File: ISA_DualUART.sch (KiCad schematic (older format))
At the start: 74 parts, among them J1 ISA BUS, J10 Parallel Port, J2 ADDR_IRQ, J3 UART1_SEL, J4 UART2_SEL, J6 Serial 2 IDC, J7 Serial 1 DB9, J9 Parport IRQ Select, U1 74LS138, U11 74LS30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

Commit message: Rerouted, now serial connector has shield to gnd
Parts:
- removed J7: Serial 1 DB9, Connector_Dsub:DSUB-9_Male_Horizontal_P2.77x2.84mm_EdgePinOffset7.70mm_Housed_MountingHolesOffset9.12mm, symbol Connector:DB9_Male
- added J7: Serial 1 DB9, Connector_Dsub:DSUB-9_Male_Horizontal_P2.77x2.84mm_EdgePinOffset7.70mm_Housed_MountingHolesOffset9.12mm, symbol Connector:DB9_Male_MountingHoles
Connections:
- wire segments 721 -> 722
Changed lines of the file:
@@
 	1500 9250 2300 9250
-$Comp
-L Connector:DB9_Male J7
-U 1 1 60F46B7A
-P 20700 3850
-F 0 "J7" H 20880 3896 50  0000 L CNN
-F 1 "Serial 1 DB9" H 20880 3805 50  0000 L CNN
-F 2 "Connector_Dsub:DSUB-9_Male_Horizontal_P2.77x2.84mm_EdgePinOffset7.70mm_Housed_MountingHolesOffset9.12mm" H 20700 3850 50  0001 C CNN
-F 3 " ~" H 20700 3850 50  0001 C CNN
-	1    20700 3850
-	1    0    0    -1
-$EndComp
 $Comp
 L power:GND #PWR0134
@@
 Wire Notes Line
 	22700 14700 22700 5350
+$Comp
+L Connector:DB9_Male_MountingHoles J7
+U 1 1 603C93D6
+P 20700 3850
+F 0 "J7" H 20880 3852 50  0000 L CNN
+F 1 "Serial 1 DB9" H 20880 3761 50  0000 L CNN
+F 2 "Connector_Dsub:DSUB-9_Male_Horizontal_P2.77x2.84mm_EdgePinOffset7.70mm_Housed_MountingHolesOffset9.12mm" H 20700 3850 50  0001 C CNN
+F 3 " ~" H 20700 3850 50  0001 C CNN
+	1    20700 3850
+	1    0    0    -1
+$EndComp
+$Comp
+L power:GND #PWR?
+U 1 1 60471E81
+P 20700 4600
+F 0 "#PWR?" H 20700 4350 50  0001 C CNN
+F 1 "GND" H 20705 4427 50  0000 C CNN
+F 2 "" H 20700 4600 50  0001 C CNN
+F 3 "" H 20700 4600 50  0001 C CNN
+	1    20700 4600
+	1    0    0    -1
+$EndComp
+Wire Wire Line
+	20700 4450 20700 4600
 Wire Bus Line
 	13800 7800 13800 13500

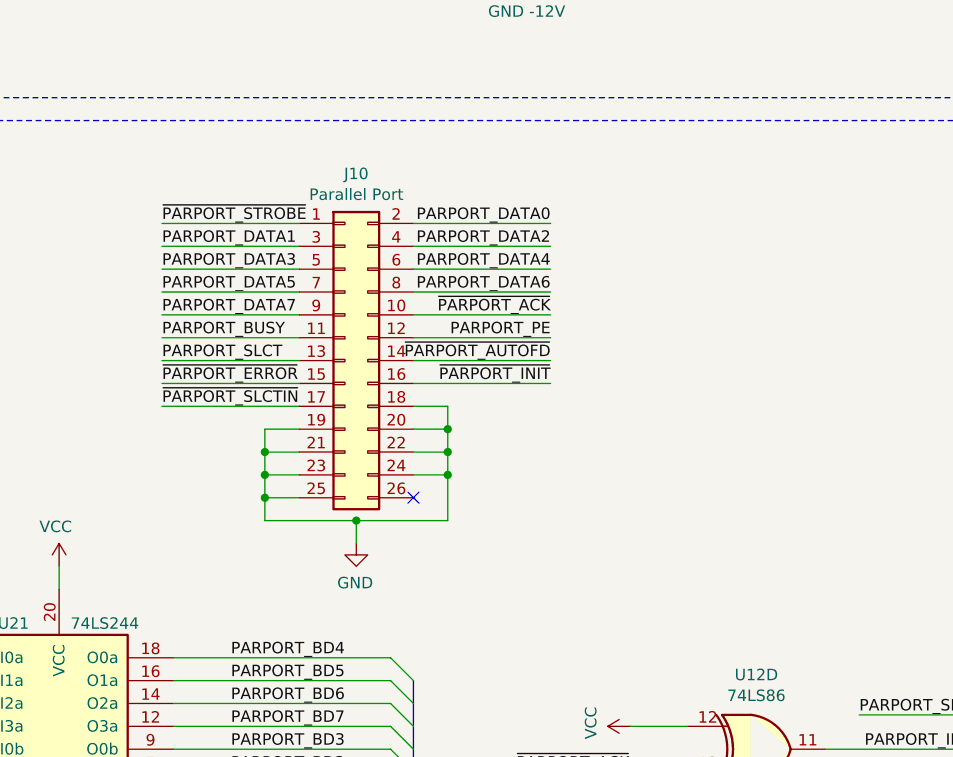
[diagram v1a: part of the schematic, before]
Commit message: Rewire parallel port connector
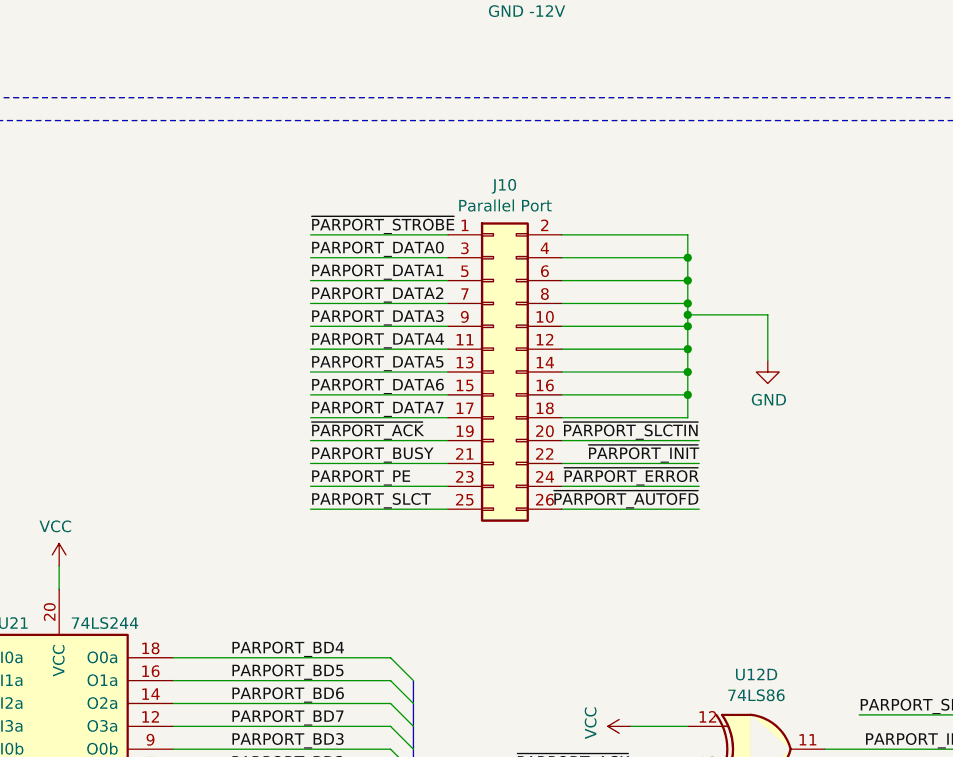
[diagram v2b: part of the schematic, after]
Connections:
- net GND: now also J10.10 (Pin_10), J10.12 (Pin_12), J10.14 (Pin_14), J10.16 (Pin_16), J10.2 (Pin_2), J10.4 (Pin_4), J10.6 (Pin_6), J10.8 (Pin_8); no longer J10.19 (Pin_19), J10.20 (Pin_20), J10.21 (Pin_21), J10.22 (Pin_22), J10.23 (Pin_23), J10.24 (Pin_24), J10.25 (Pin_25)
- net PARPORT_BUSY: now also J10.21 (Pin_21); no longer J10.11 (Pin_11)
- net PARPORT_DATA0: now also J10.3 (Pin_3); no longer J10.2 (Pin_2)
- net PARPORT_DATA1: now also J10.5 (Pin_5); no longer J10.3 (Pin_3)
- net PARPORT_DATA2: now also J10.7 (Pin_7); no longer J10.4 (Pin_4)
- net PARPORT_DATA3: now also J10.9 (Pin_9); no longer J10.5 (Pin_5)
- net PARPORT_DATA4: now also J10.11 (Pin_11); no longer J10.6 (Pin_6)
- net PARPORT_DATA5: now also J10.13 (Pin_13); no longer J10.7 (Pin_7)
- net PARPORT_DATA6: now also J10.15 (Pin_15); no longer J10.8 (Pin_8)
- net PARPORT_DATA7: now also J10.17 (Pin_17); no longer J10.9 (Pin_9)
- net PARPORT_PE: now also J10.23 (Pin_23); no longer J10.12 (Pin_12)
- net PARPORT_SLCT: now also J10.25 (Pin_25); no longer J10.13 (Pin_13)
- net ~PARPORT_ACK: now also J10.19 (Pin_19); no longer J10.10 (Pin_10)
- net ~PARPORT_AUTOFD: now also J10.26 (Pin_26); no longer J10.14 (Pin_14)
- net ~PARPORT_ERROR: now also J10.24 (Pin_24); no longer J10.15 (Pin_15)
- net ~PARPORT_INIT: now also J10.22 (Pin_22); no longer J10.16 (Pin_16)
- net ~PARPORT_SLCTIN: now also J10.20 (Pin_20); no longer J10.17 (Pin_17)
- no-connect marks 43 -> 42
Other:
- moved on the sheet: J10
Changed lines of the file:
@@
 Wire Bus Line
 	7650 13500 13800 13500
-$Comp
-L 74xx:74LS244 U21
-U 1 1 6EEE2F98
-P 12250 8200
-F 0 "U21" H 12050 8850 50  0000 C CNN
-F 1 "74LS244" H 12450 8850 50  0000 C CNN
-F 2 "Package_DIP:DIP-20_W7.62mm_LongPads" H 12250 8200 50  0001 C CNN
-F 3 "http://www.ti.com/lit/ds/symlink/sn74ls244.pdf" H 12250 8200 50  0001 C CNN
-	1    12250 8200
-	1    0    0    -1
-$EndComp
 Wire Wire Line
 	12250 7300 12250 7400
@@
 L Connector_Generic:Conn_02x13_Odd_Even J10
 U 1 1 7146EF36
-P 13500 6400
-F 0 "J10" H 13550 7217 50  0000 C CNN
-F 1 "Parallel Port" H 13550 7126 50  0000 C CNN
-F 2 "Connector_PinHeader_2.54mm:PinHeader_2x13_P2.54mm_Vertical" H 13500 6400 50  0001 C CNN
-F 3 "~" H 13500 6400 50  0001 C CNN
-	1    13500 6400
-	1    0    0    -1
-$EndComp
-NoConn ~ 13800 7000
-Wire Wire Line
-	13300 6700 13150 6700
-Wire Wire Line
-	13300 6800 13150 6800
-Wire Wire Line
-	13300 6900 13150 6900
-Wire Wire Line
-	13300 7000 13150 7000
-Wire Wire Line
-	13950 6600 13800 6600
-Wire Wire Line
-	13950 6700 13800 6700
-Wire Wire Line
-	13950 6800 13800 6800
-Wire Wire Line
-	13950 6900 13800 6900
-Wire Wire Line
-	13950 6600 13950 6700
-Wire Wire Line
-	13950 6700 13950 6800
-Connection ~ 13950 6700
-Wire Wire Line
-	13950 6800 13950 6900
-Connection ~ 13950 6800
-Wire Wire Line
-	13150 6700 13150 6800
-Wire Wire Line
-	13150 6800 13150 6900
-Connection ~ 13150 6800
-Wire Wire Line
-	13150 6900 13150 7000
-Connection ~ 13150 6900
-Wire Wire Line
-	13950 6900 13950 7100
-Wire Wire Line
-	13950 7100 13550 7100
-Wire Wire Line
-	13150 7100 13150 7000
-Connection ~ 13950 6900
-Connection ~ 13150 7000
-$Comp
-L power:GND #PWR0204
-U 1 1 72044B44
-P 13550 7200
-F 0 "#PWR0204" H 13550 6950 50  0001 C CNN
-F 1 "GND" H 13555 7027 50  0000 C CNN
-F 2 "" H 13550 7200 50  0001 C CNN
-F 3 "" H 13550 7200 50  0001 C CNN
-	1    13550 7200
-	-1   0    0    -1
-$EndComp
-Wire Wire Line
-	13550 7100 13550 7200
-Connection ~ 13550 7100
-Wire Wire Line
-	13550 7100 13150 7100
-Wire Wire Line
-	13300 5800 12700 5800
-Wire Wire Line
-	13300 5900 12700 5900
-Wire Wire Line
-	13300 6000 12700 6000
-Wire Wire Line
-	13300 6100 12700 6100
-Wire Wire Line
-	13300 6200 12700 6200
-Wire Wire Line
-	13300 6300 12700 6300
-Wire Wire Line
-	13300 6400 12700 6400
-Wire Wire Line
-	13300 6500 12700 6500
-Wire Wire Line
-	13300 6600 12700 6600
-Wire Wire Line
-	14400 5800 13800 5800
-Wire Wire Line
-	14400 5900 13800 5900
-Wire Wire Line
-	14400 6000 13800 6000
-Wire Wire Line
-	14400 6100 13800 6100
-Wire Wire Line
-	14400 6200 13800 6200
-Wire Wire Line
-	14400 6300 13800 6300
-Wire Wire Line
-	14400 6400 13800 6400
-Wire Wire Line
-	14400 6500 13800 6500
-Text Label 12700 5800 0    50   ~ 0
+P 14150 6450
+F 0 "J10" H 14200 7267 50  0000 C CNN
+F 1 "Parallel Port" H 14200 7176 50  0000 C CNN
+F 2 "Connector_PinHeader_2.54mm:PinHeader_2x13_P2.54mm_Vertical" H 14150 6450 50  0001 C CNN
+F 3 "~" H 14150 6450 50  0001 C CNN
+	1    14150 6450
+	1    0    0    -1
+$EndComp
+Wire Wire Line
+	13950 5850 13350 5850
+Wire Wire Line
+	13950 6050 13350 6050
+Wire Wire Line
+	13950 6250 13350 6250
+Wire Wire Line
+	13950 6450 13350 6450
+Wire Wire Line
+	13950 6650 13350 6650
+Wire Wire Line
+	13950 6850 13350 6850
+Wire Wire Line
+	13950 7050 13350 7050
+Wire Wire Line
+	14450 6950 15050 6950
+Wire Wire Line
+	14450 6750 15050 6750
+Wire Wire Line
+	13350 5950 13950 5950
+Wire Wire Line
+	13350 6150 13950 6150
+Wire Wire Line
+	13350 6350 13950 6350
+Wire Wire Line
+	13350 6550 13950 6550
+Wire Wire Line
+	13350 6750 13950 6750
+Wire Wire Line
+	13350 6950 13950 6950
+Wire Wire Line
+	15050 7050 14450 7050
+Wire Wire Line
+	15050 6850 14450 6850
+Text Label 13350 5850 0    50   ~ 0
 ~PARPORT_STROBE
-Text Label 12700 5900 0    50   ~ 0
+Text Label 13350 6050 0    50   ~ 0
 PARPORT_DATA1
-Text Label 12700 6000 0    50   ~ 0
+Text Label 13350 6250 0    50   ~ 0
 PARPORT_DATA3
-Text Label 12700 6100 0    50   ~ 0
+Text Label 13350 6450 0    50   ~ 0
 PARPORT_DATA5
-Text Label 12700 6200 0    50   ~ 0
+Text Label 13350 6650 0    50   ~ 0
 PARPORT_DATA7
-Text Label 14400 5800 2    50   ~ 0
+Text Label 13350 5950 0    50   ~ 0
 PARPORT_DATA0
-Text Label 14400 5900 2    50   ~ 0
+Text Label 13350 6150 0    50   ~ 0
 PARPORT_DATA2
-Text Label 14400 6000 2    50   ~ 0
+Text Label 13350 6350 0    50   ~ 0
 PARPORT_DATA4
-Text Label 14400 6100 2    50   ~ 0
+Text Label 13350 6550 0    50   ~ 0
 PARPORT_DATA6
-Text Label 12700 6300 0    50   ~ 0
+Text Label 13350 6850 0    50   ~ 0
 PARPORT_BUSY
-Text Label 12700 6400 0    50   ~ 0
+Text Label 13350 7050 0    50   ~ 0
 PARPORT_SLCT
-Text Label 12700 6500 0    50   ~ 0
+Text Label 15050 6950 2    50   ~ 0
 ~PARPORT_ERROR
-Text Label 12700 6600 0    50   ~ 0
+Text Label 15050 6750 2    50   ~ 0
 ~PARPORT_SLCTIN
-Text Label 14400 6200 2    50   ~ 0
+Text Label 13350 6750 0    50   ~ 0
 ~PARPORT_ACK
-Text Label 14400 6300 2    50   ~ 0
+Text Label 13350 6950 0    50   ~ 0
 PARPORT_PE
-Text Label 14400 6400 2    50   ~ 0
+Text Label 15050 7050 2    50   ~ 0
 ~PARPORT_AUTOFD
-Text Label 14400 6500 2    50   ~ 0
+Text Label 15050 6850 2    50   ~ 0
 ~PARPORT_INIT
 $Comp
@@
 Wire Wire Line
 	20700 4450 20700 4600
+Wire Wire Line
+	14450 5850 15000 5850
+Wire Wire Line
+	14450 5950 15000 5950
+Wire Wire Line
+	14450 6050 15000 6050
+Wire Wire Line
+	14450 6150 15000 6150
+Wire Wire Line
+	14450 6250 15000 6250
+Wire Wire Line
+	14450 6350 15000 6350
+Wire Wire Line
+	14450 6450 15000 6450
+Wire Wire Line
+	14450 6550 15000 6550
+Wire Wire Line
+	14450 6650 15000 6650
+Wire Wire Line
+	15000 5850 15000 5950
+Wire Wire Line
+	15000 6050 15000 5950
+Connection ~ 15000 5950
+Wire Wire Line
+	15000 6050 15000 6150
+Connection ~ 15000 6050
+Wire Wire Line
+	15000 6150 15000 6200
+Connection ~ 15000 6150
+Wire Wire Line
+	15000 6250 15000 6350
+Connection ~ 15000 6250
+Wire Wire Line
+	15000 6350 15000 6450
+Connection ~ 15000 6350
+Wire Wire Line
+	15000 6450 15000 6550
+Connection ~ 15000 6450
+Wire Wire Line
+	15000 6550 15000 6650
+Connection ~ 15000 6550
+Wire Wire Line
+	15000 6200 15350 6200
+Wire Wire Line
+	15350 6200 15350 6400
+Connection ~ 15000 6200
+Wire Wire Line
+	15000 6200 15000 6250
+$Comp
+L power:GND #PWR?
+U 1 1 635BB839
+P 15350 6400
+F 0 "#PWR?" H 15350 6150 50  0001 C CNN
+F 1 "GND" H 15355 6227 50  0000 C CNN
+F 2 "" H 15350 6400 50  0001 C CNN
+F 3 "" H 15350 6400 50  0001 C CNN
+	1    15350 6400
+	1    0    0    -1
+$EndComp
+$Comp
+L 74xx:74LS244 U21
+U 1 1 6EEE2F98
+P 12250 8200
+F 0 "U21" H 12050 8850 50  0000 C CNN
+F 1 "74LS244" H 12450 8850 50  0000 C CNN
+F 2 "Package_DIP:DIP-20_W7.62mm_LongPads" H 12250 8200 50  0001 C CNN
+F 3 "http://www.ti.com/lit/ds/symlink/sn74ls244.pdf" H 12250 8200 50  0001 C CNN
+	1    12250 8200
+	1    0    0    -1
+$EndComp
 Wire Bus Line
 	13800 7800 13800 13500

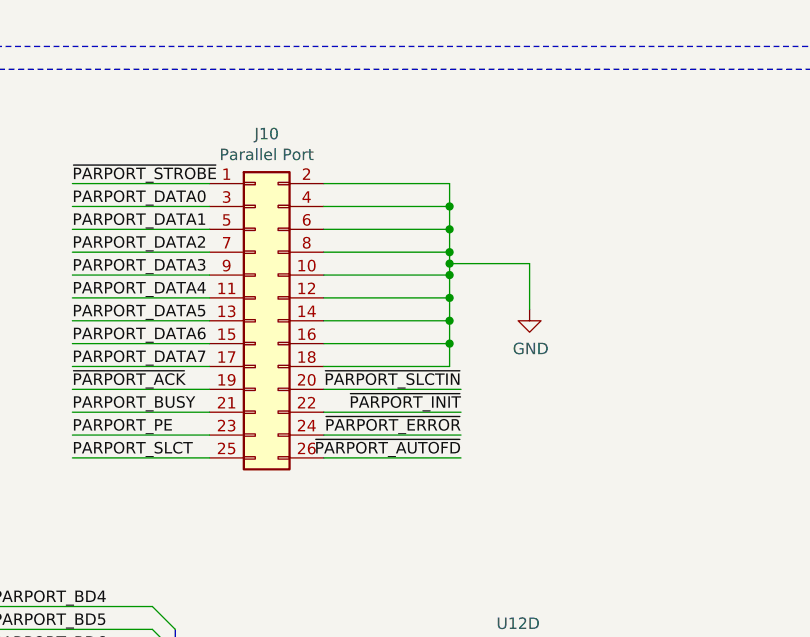
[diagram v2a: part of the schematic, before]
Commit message: Changed organization of parport connector
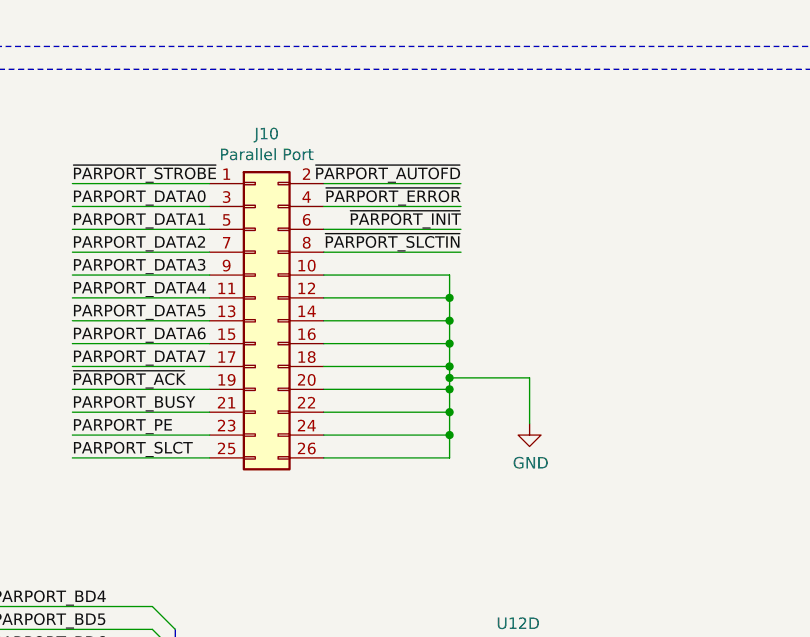
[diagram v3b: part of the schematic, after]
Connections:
- net GND: now also J10.20 (Pin_20), J10.22 (Pin_22), J10.24 (Pin_24), J10.26 (Pin_26); no longer J10.2 (Pin_2), J10.4 (Pin_4), J10.6 (Pin_6), J10.8 (Pin_8)
- net ~PARPORT_AUTOFD: now also J10.2 (Pin_2); no longer J10.26 (Pin_26)
- net ~PARPORT_ERROR: now also J10.4 (Pin_4); no longer J10.24 (Pin_24)
- net ~PARPORT_INIT: now also J10.6 (Pin_6); no longer J10.22 (Pin_22)
- net ~PARPORT_SLCTIN: now also J10.8 (Pin_8); no longer J10.20 (Pin_20)
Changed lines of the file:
@@
 	13950 7050 13350 7050
 Wire Wire Line
-	14450 6950 15050 6950
-Wire Wire Line
-	14450 6750 15050 6750
+	14450 5950 15050 5950
+Wire Wire Line
+	14450 6150 15050 6150
 Wire Wire Line
 	13350 5950 13950 5950
@@
 	13350 6950 13950 6950
 Wire Wire Line
-	15050 7050 14450 7050
-Wire Wire Line
-	15050 6850 14450 6850
+	15050 5850 14450 5850
+Wire Wire Line
+	15050 6050 14450 6050
 Text Label 13350 5850 0    50   ~ 0
 ~PARPORT_STROBE
@@
 Text Label 13350 7050 0    50   ~ 0
 PARPORT_SLCT
-Text Label 15050 6950 2    50   ~ 0
+Text Label 15050 5950 2    50   ~ 0
 ~PARPORT_ERROR
-Text Label 15050 6750 2    50   ~ 0
+Text Label 15050 6150 2    50   ~ 0
 ~PARPORT_SLCTIN
 Text Label 13350 6750 0    50   ~ 0
@@
 Text Label 13350 6950 0    50   ~ 0
 PARPORT_PE
-Text Label 15050 7050 2    50   ~ 0
+Text Label 15050 5850 2    50   ~ 0
 ~PARPORT_AUTOFD
-Text Label 15050 6850 2    50   ~ 0
+Text Label 15050 6050 2    50   ~ 0
 ~PARPORT_INIT
 $Comp
@@
 $EndComp
 $Comp
-L power:GND #PWR?
+L power:GND #PWR0146
 U 1 1 60471E81
 P 20700 4600
-F 0 "#PWR?" H 20700 4350 50  0001 C CNN
+F 0 "#PWR0146" H 20700 4350 50  0001 C CNN
 F 1 "GND" H 20705 4427 50  0000 C CNN
 F 2 "" H 20700 4600 50  0001 C CNN
@@
 	20700 4450 20700 4600
 Wire Wire Line
-	14450 5850 15000 5850
-Wire Wire Line
-	14450 5950 15000 5950
-Wire Wire Line
-	14450 6050 15000 6050
-Wire Wire Line
-	14450 6150 15000 6150
+	14450 7050 15000 7050
+Wire Wire Line
+	14450 6950 15000 6950
+Wire Wire Line
+	14450 6850 15000 6850
+Wire Wire Line
+	14450 6750 15000 6750
+Wire Wire Line
+	14450 6650 15000 6650
+Wire Wire Line
+	14450 6550 15000 6550
+Wire Wire Line
+	14450 6450 15000 6450
+Wire Wire Line
+	14450 6350 15000 6350
 Wire Wire Line
 	14450 6250 15000 6250
 Wire Wire Line
-	14450 6350 15000 6350
-Wire Wire Line
-	14450 6450 15000 6450
-Wire Wire Line
-	14450 6550 15000 6550
-Wire Wire Line
-	14450 6650 15000 6650
-Wire Wire Line
-	15000 5850 15000 5950
-Wire Wire Line
-	15000 6050 15000 5950
-Connection ~ 15000 5950
-Wire Wire Line
-	15000 6050 15000 6150
-Connection ~ 15000 6050
-Wire Wire Line
-	15000 6150 15000 6200
-Connection ~ 15000 6150
-Wire Wire Line
-	15000 6250 15000 6350
-Connection ~ 15000 6250
-Wire Wire Line
-	15000 6350 15000 6450
+	15000 7050 15000 6950
+Wire Wire Line
+	15000 6850 15000 6950
+Connection ~ 15000 6950
+Wire Wire Line
+	15000 6850 15000 6750
+Connection ~ 15000 6850
+Wire Wire Line
+	15000 6750 15000 6700
+Connection ~ 15000 6750
+Wire Wire Line
+	15000 6650 15000 6550
+Connection ~ 15000 6650
+Wire Wire Line
+	15000 6550 15000 6450
+Connection ~ 15000 6550
+Wire Wire Line
+	15000 6450 15000 6350
+Connection ~ 15000 6450
+Wire Wire Line
+	15000 6350 15000 6250
 Connection ~ 15000 6350
 Wire Wire Line
-	15000 6450 15000 6550
-Connection ~ 15000 6450
-Wire Wire Line
-	15000 6550 15000 6650
-Connection ~ 15000 6550
-Wire Wire Line
-	15000 6200 15350 6200
-Wire Wire Line
-	15350 6200 15350 6400
-Connection ~ 15000 6200
-Wire Wire Line
-	15000 6200 15000 6250
-$Comp
-L power:GND #PWR?
+	15000 6700 15350 6700
+Wire Wire Line
+	15350 6700 15350 6900
+Connection ~ 15000 6700
+Wire Wire Line
+	15000 6700 15000 6650
+$Comp
+L power:GND #PWR0147
 U 1 1 635BB839
-P 15350 6400
-F 0 "#PWR?" H 15350 6150 50  0001 C CNN
-F 1 "GND" H 15355 6227 50  0000 C CNN
-F 2 "" H 15350 6400 50  0001 C CNN
-F 3 "" H 15350 6400 50  0001 C CNN
-	1    15350 6400
-	1    0    0    -1
-$EndComp
+P 15350 6900
+F 0 "#PWR0147" H 15350 6650 50  0001 C CNN
+F 1 "GND" H 15355 6727 50  0000 C CNN
+F 2 "" H 15350 6900 50  0001 C CNN
+F 3 "" H 15350 6900 50  0001 C CNN
+	1    15350 6900
+	1    0    0    -1
+$EndComp

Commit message: Invert IRQ sensing to conform to AT specs
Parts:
- added R16: 4.7k, Resistor_THT:R_Axial_DIN0207_L6.3mm_D2.5mm_P10.16mm_Horizontal, symbol Device:R_Small
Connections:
- net PARPORT_IRQ: no longer U19.12
- net VCC: now also R16.1
- net ~PARPORT_ACK: now also U19.12, R16.2
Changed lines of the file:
@@
 	14750 8000 15000 8000
 Wire Wire Line
-	15000 8200 14250 8200
+	15000 8200 14750 8200
 Text Label 14250 8200 0    50   ~ 0
 ~PARPORT_ACK
@@
 Text Label 14550 9150 0    50   ~ 0
 ~PARPORT_IRQEN
-Wire Wire Line
-	16350 8100 16350 8350
-Wire Wire Line
-	16350 8350 14750 8350
-Wire Wire Line
-	14750 8350 14750 8750
 Wire Wire Line
 	14750 8750 15000 8750
@@
 Wire Wire Line
 	18800 8700 16350 8700
-Wire Wire Line
-	16350 8700 16350 8350
-Connection ~ 16350 8350
 Text Label 18050 9200 0    50   ~ 0
 ~PARPORT_STROBE
@@
 	1    0    0    -1
 $EndComp
+$Comp
+L Device:R_Small R16
+U 1 1 63A381BF
+P 14450 8750
+F 0 "R16" V 14550 8850 50  0000 C CNN
+F 1 "4.7k" V 14550 8650 50  0000 C CNN
+F 2 "Resistor_THT:R_Axial_DIN0207_L6.3mm_D2.5mm_P10.16mm_Horizontal" H 14450 8750 50  0001 C CNN
+F 3 "~" H 14450 8750 50  0001 C CNN
+	1    14450 8750
+	0    -1   -1   0
+$EndComp
+Wire Wire Line
+	14250 8750 14350 8750
+$Comp
+L power:VCC #PWR?
+U 1 1 63A3972E
+P 14250 8750
+F 0 "#PWR?" H 14250 8600 50  0001 C CNN
+F 1 "VCC" H 14265 8923 50  0000 C CNN
+F 2 "" H 14250 8750 50  0001 C CNN
+F 3 "" H 14250 8750 50  0001 C CNN
+	1    14250 8750
+	0    -1   -1   0
+$EndComp
+Wire Wire Line
+	16350 8100 16350 8700
+Wire Wire Line
+	14750 8750 14750 8200
+Connection ~ 14750 8200
+Wire Wire Line
+	14750 8200 14250 8200
+Wire Wire Line
+	14550 8750 14750 8750
 Wire Bus Line
 	13800 7800 13800 13500
@@
 Wire Bus Line
 	7650 9100 7650 13500
+Connection ~ 14750 8750
 $EndSCHEMATC
